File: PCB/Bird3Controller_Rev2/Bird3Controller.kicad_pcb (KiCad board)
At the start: 2 copper layers, 43 x 108 mm, 50 parts, among them J1 Bird 3 24-pin Connector, J2 TXW154028S0 Connector, J3 87832-2220, Q1 2N7002A, SW1 SW_Boot, SW2 SW_Reset, U1 ESP32-S3-WROOM-1, U3 SN65HVD231, U4 LMR36520ADDAR, U5 LM3519MK-20_NOPB

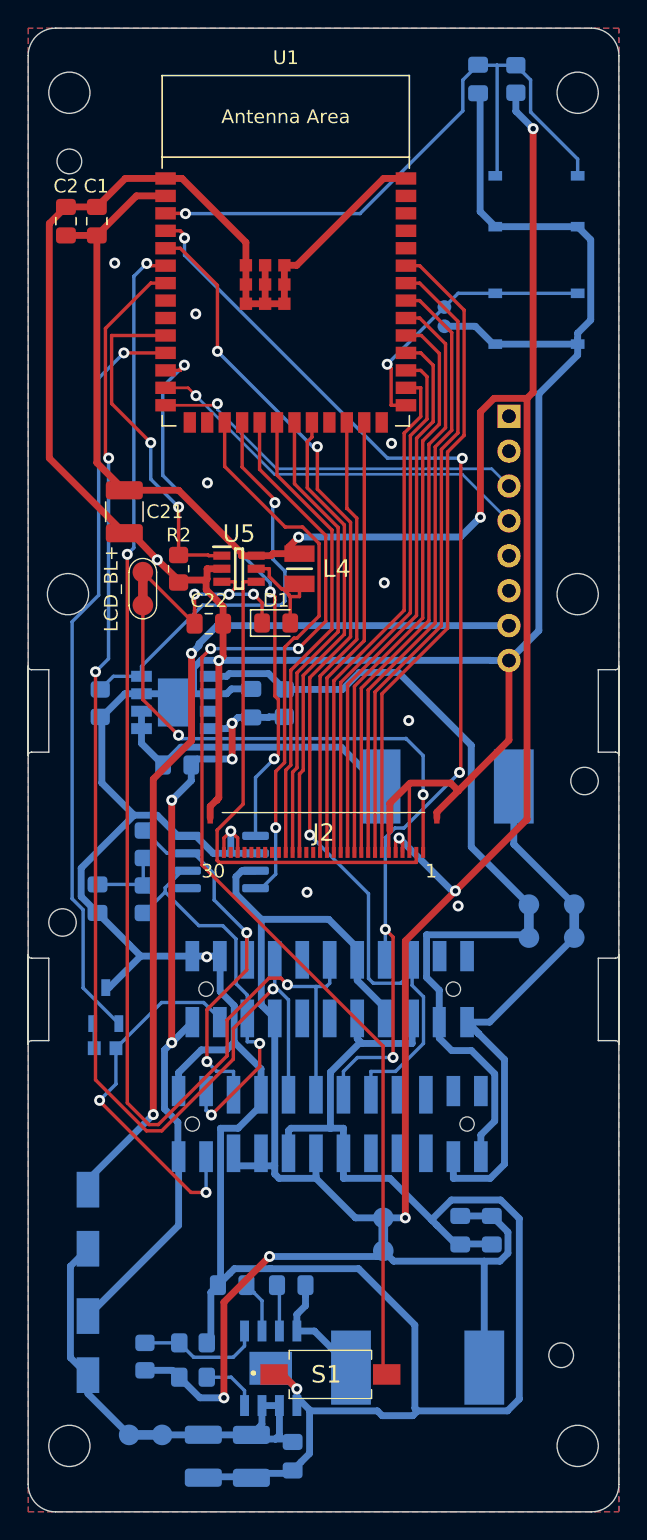
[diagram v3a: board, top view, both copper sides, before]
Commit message: Update PCB to use add PTC fuse on VIN
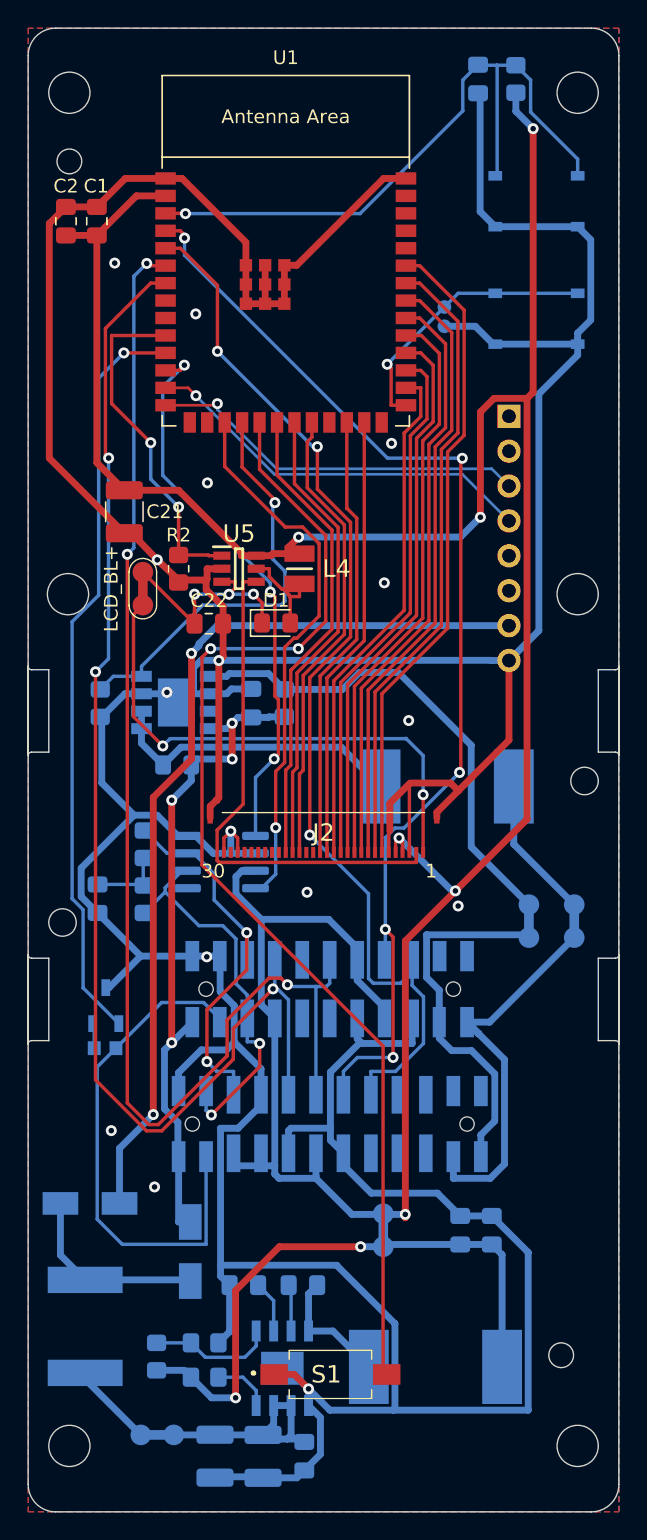
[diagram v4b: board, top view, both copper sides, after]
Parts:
- added F2: 0ZCF0100AF2A, Bird3Controller:FUSC7451X170N, B.Cu at (164.7, 136.5)
- moved D5 10.1 mm to (172.3, 131.1)
- moved L3 1.30 mm to (190.2, 139.4)
- moved D6 1.16 mm to (165.0, 127.5), turned to 0 degrees
- moved C14 0.85 mm to (177.6, 146.0)
- moved C15 0.85 mm to (180.6, 145.9)
- moved C16 0.85 mm to (174.1, 145.9)
- moved C17 0.85 mm to (176.2, 133.5)
- moved C19 0.85 mm to (180.5, 133.5)
- moved R11 0.85 mm to (173.3, 140.2)
- moved R12 0.85 mm to (169.8, 138.7)
- moved R13 0.85 mm to (173.3, 137.7)
- moved TP3 0.85 mm to (169.9, 144.4)
- moved U4 0.85 mm to (179.0, 139.6)
- moved TP2 0.30 mm to (186.3, 129.5)
- turned C18 to 90 degrees
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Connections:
- TP3 pad 2: Net-(D5-K) -> Net-(F2-Pad2)
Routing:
- net /PWR_ENA: track 27.2 -> 37.8 mm, vias 2 -> 0
- net GND: track 421.8 -> 412.2 mm, vias 13 -> 16
- net +36V: track 59.7 -> 50.1 mm
- net Net-(F2-Pad2): track 0.00 -> 6.19 mm
- net Net-(C18-Pad1): track 49.6 -> 43.7 mm
- net /LCD_BL+: track 36.0 -> 38.2 mm
- net Net-(D5-K): track 15.8 -> 14.0 mm

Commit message: Label USB connector pins
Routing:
- net +3V3: track 220.1 -> 220.9 mm
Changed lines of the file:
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@@
         (effects (font (size 1 1) (thickness 0.15)) (justify mirror))
+    )
+    (fp_text user "SBU1" (at 1.15 -2.55 unlocked) (layer "B.SilkS")
+        (effects (font (size 1 1) (thickness 0.25) bold) (justify left mirror))
+    )
+    (fp_text user "D-" (at 1.15 -7.65 unlocked) (layer "B.SilkS")
+        (effects (font (size 1 1) (thickness 0.25) bold) (justify left mirror))
+    )
+    (fp_text user "D+" (at 1.15 -5.1 unlocked) (layer "B.SilkS")
+        (effects (font (size 1 1) (thickness 0.25) bold) (justify left mirror))
+    )
+    (fp_text user "GND" (at 1.15 -17.85 unlocked) (layer "B.SilkS")
+        (effects (font (size 1 1) (thickness 0.25) bold) (justify left mirror))
+    )
+    (fp_text user "CC2" (at 1.15 0 unlocked) (layer "B.SilkS")
+        (effects (font (size 1 1) (thickness 0.25) bold) (justify left mirror))
+    )
+    (fp_text user "CC1" (at 1.15 -10.15 unlocked) (layer "B.SilkS")
+        (effects (font (size 1 1) (thickness 0.25) bold) (justify left mirror))
+    )
+    (fp_text user "+5V" (at 1.15 -15.25 unlocked) (layer "B.SilkS")
+        (effects (font (size 1 1) (thickness 0.25) bold) (justify left mirror))
+    )
+    (fp_text user "SBU2" (at 1.15 -12.7 unlocked) (layer "B.SilkS")
+        (effects (font (size 1 1) (thickness 0.25) bold) (justify left mirror))
+    )
+    (fp_text user "SBU1" (at 1.15 -2.55 unlocked) (layer "F.SilkS")
+        (effects (font (size 1 1) (thickness 0.25) bold) (justify right))
+    )
+    (fp_text user "+5V" (at 1.15 -15.25 unlocked) (layer "F.SilkS")
+        (effects (font (size 1 1) (thickness 0.25) bold) (justify right))
+    )
+    (fp_text user "D+" (at 1.15 -5.1 unlocked) (layer "F.SilkS")
+        (effects (font (size 1 1) (thickness 0.25) bold) (justify right))
+    )
+    (fp_text user "SBU2" (at 1.15 -12.7 unlocked) (layer "F.SilkS")
+        (effects (font (size 1 1) (thickness 0.25) bold) (justify right))
+    )
+    (fp_text user "D-" (at 1.15 -7.65 unlocked) (layer "F.SilkS")
+        (effects (font (size 1 1) (thickness 0.25) bold) (justify right))
+    )
+    (fp_text user "CC1" (at 1.15 -10.15 unlocked) (layer "F.SilkS")
+        (effects (font (size 1 1) (thickness 0.25) bold) (justify right))
+    )
+    (fp_text user "CC2" (at 1.15 0 unlocked) (layer "F.SilkS")
+        (effects (font (size 1 1) (thickness 0.25) bold) (justify right))
+    )
+    (fp_text user "GND" (at 1.15 -17.85 unlocked) (layer "F.SilkS")
+        (effects (font (size 1 1) (thickness 0.25) bold) (justify right))
     )
     (fp_text user "${REFERENCE}" (at 0 -8.89 90) (layer "B.Fab")
         (effects (font (size 1 1) (thickness 0.15)) (justify mirror))
     )
-    (fp_line (start -1.33 -19.11) (end 1.33 -19.11)
-      (stroke (width 0.12) (type solid)) (layer "B.SilkS"))
-    (fp_line (start -1.33 -1.27) (end -1.33 -19.11)
-      (stroke (width 0.12) (type solid)) (layer "B.SilkS"))
-    (fp_line (start -1.33 -1.27) (end 1.33 -1.27)
-      (stroke (width 0.12) (type solid)) (layer "B.SilkS"))
-    (fp_line (start -1.33 0) (end -1.33 1.33)
-      (stroke (width 0.12) (type solid)) (layer "B.SilkS"))
-    (fp_line (start -1.33 1.33) (end 0 1.33)
-      (stroke (width 0.12) (type solid)) (layer "B.SilkS"))
-    (fp_line (start 1.33 -1.27) (end 1.33 -19.11)
-      (stroke (width 0.12) (type solid)) (layer "B.SilkS"))
+    (fp_line (start -1.3 -19.1) (end 6.35 -19.1)
+      (stroke (width 0.12) (type solid)) (layer "B.SilkS"))
+    (fp_line (start -1.3 -1.25) (end -1.3 -19.1)
+      (stroke (width 0.12) (type solid)) (layer "B.SilkS"))
+    (fp_line (start -1.3 -1.25) (end 6.35 -1.25)
+      (stroke (width 0.12) (type solid)) (layer "B.SilkS"))
+    (fp_line (start -1.3 0) (end -1.3 1.33)
+      (stroke (width 0.12) (type solid)) (layer "B.SilkS"))
+    (fp_line (start -1.3 1.33) (end 0.03 1.33)
+      (stroke (width 0.12) (type solid)) (layer "B.SilkS"))
+    (fp_line (start 6.35 -1.25) (end 6.35 -19.1)
+      (stroke (width 0.12) (type solid)) (layer "B.SilkS"))
+    (fp_line (start -1.3 -19.1) (end 6.35 -19.1)
+      (stroke (width 0.12) (type solid)) (layer "F.SilkS"))
+    (fp_line (start -1.3 -1.25) (end -1.3 -19.1)
+      (stroke (width 0.12) (type solid)) (layer "F.SilkS"))
+    (fp_line (start -1.3 -1.25) (end 6.35 -1.25)
+      (stroke (width 0.12) (type solid)) (layer "F.SilkS"))
+    (fp_line (start -1.3 0) (end -1.3 1.33)
+      (stroke (width 0.12) (type solid)) (layer "F.SilkS"))
+    (fp_line (start -1.3 1.33) (end 0.03 1.33)
+      (stroke (width 0.12) (type solid)) (layer "F.SilkS"))
+    (fp_line (start 6.35 -1.25) (end 6.35 -19.1)
+      (stroke (width 0.12) (type solid)) (layer "F.SilkS"))
     (fp_line (start -1.8 -19.55) (end 1.8 -19.55)
       (stroke (width 0.05) (type solid)) (layer "B.CrtYd"))
@@
     (fp_line (start 1.27 -19.05) (end -1.27 -19.05)
       (stroke (width 0.1) (type solid)) (layer "B.Fab"))
-    (fp_line (start 1.27 1.27) (end 1.27 -19.05)
+    (fp_line (start 6.35 1.27) (end 6.35 -19.05)
       (stroke (width 0.1) (type solid)) (layer "B.Fab"))
     (pad "1" thru_hole rect (at 0 0 180) (size 1.7 1.7) (drill 1) (layers "*.Cu" "*.Mask")
@@
   (segment (start 190.25 99.0739) (end 191.812 97.5119) (width 0.5) (layer "F.Cu") (net 5))
   (via (at 166.55 122.25) (size 0.8) (drill 0.4) (layers "F.Cu" "B.Cu") (free) (net 5))
-  (via (at 191.8 105.9) (size 0.8) (drill 0.4) (layers "F.Cu" "B.Cu") (free) (net 5))
+  (via (at 193.65 106.05) (size 0.8) (drill 0.4) (layers "F.Cu" "B.Cu") (free) (net 5))
   (via (at 170.6 90.35) (size 0.8) (drill 0.4) (layers "F.Cu" "B.Cu") (net 5))
   (via (at 169.9 80.7) (size 0.8) (drill 0.4) (layers "F.Cu" "B.Cu") (net 5))
@@
   (segment (start 180.25 80.25) (end 179.474 80.25) (width 0.5) (layer "F.Cu") (net 9))
   (segment (start 178.327 80.25) (end 178.177 80.4) (width 0.5) (layer "F.Cu") (net 9))
+  (segment (start 193.42 69.9422) (end 194.414 68.9481) (width 0.5) (layer "F.Cu") (net 9))
   (segment (start 187.75 102) (end 187.75 101.4) (width 0.25) (layer "F.Cu") (net 9))
+  (segment (start 187.5 101.2) (end 187.7 101.4) (width 0) (layer "F.Cu") (net 9))
+  (segment (start 193.42 79.03) (end 193.42 69.9422) (width 0.5) (layer "F.Cu") (net 9))
+  (segment (start 191.6 104.8) (end 187.956 108.444) (width 0.5) (layer "F.Cu") (net 9))
   (segment (start 194.414 68.9481) (end 196.814 68.9481) (width 0.5) (layer "F.Cu") (net 9))
-  (segment (start 187.5 101.2) (end 187.7 101.4) (width 0) (layer "F.Cu") (net 9))
-  (segment (start 193.42 77.6) (end 193.42 69.9422) (width 0.5) (layer "F.Cu") (net 9))
-  (segment (start 191.6 104.8) (end 187.956 108.444) (width 0.5) (layer "F.Cu") (net 9))
   (segment (start 179.474 80.25) (end 178.327 80.25) (width 0.5) (layer "F.Cu") (net 9))
   (segment (start 165.5 57.0875) (end 163.25 57.0875) (width 0.5) (layer "F.Cu") (net 9))
@@
   (segment (start 165.5 57.0875) (end 165.5 73.6375) (width 0.5) (layer "F.Cu") (net 9))
   (segment (start 178.177 80.4) (end 177.1 80.4) (width 0.5) (layer "F.Cu") (net 9))
-  (segment (start 193.42 69.9422) (end 194.414 68.9481) (width 0.5) (layer "F.Cu") (net 9))
   (segment (start 179.474 79.765904) (end 180.188337 79.051567) (width 0.5) (layer "F.Cu") (net 9))
   (segment (start 187.956 108.444) (end 187.956 128.594) (width 0.5) (layer "F.Cu") (net 9))
@@
   (segment (start 176.023 80.4) (end 176.023 80.212) (width 0.5) (layer "F.Cu") (net 9))
   (segment (start 165.5 73.6375) (end 167.5 75.6375) (width 0.5) (layer "F.Cu") (net 9))
+  (segment (start 193.4 79.05) (end 193.42 79.03) (width 0.5) (layer "F.Cu") (net 9))
   (segment (start 176.023 80.212) (end 171.449 75.6375) (width 0.5) (layer "F.Cu") (net 9))
   (segment (start 197.258 68.5036) (end 197.258 49.3183) (width 0.5) (layer "F.Cu") (net 9))
@@
   (via (at 187.95 128.35) (size 0.8) (drill 0.4) (layers "F.Cu" "B.Cu") (net 9))
   (via (at 191.6 104.8) (size 0.8) (drill 0.4) (layers "F.Cu" "B.Cu") (net 9))
-  (via (at 193.42 77.6) (size 0.8) (drill 0.4) (layers "F.Cu" "B.Cu") (net 9))
+  (via (at 193.4 79.05) (size 0.8) (drill 0.4) (layers "F.Cu" "B.Cu") (net 9))
   (via (at 180.188337 79.051567) (size 0.8) (drill 0.4) (layers "F.Cu" "B.Cu") (net 9))
   (via (at 197.258 49.3183) (size 0.8) (drill 0.4) (layers "F.Cu" "B.Cu") (net 9))
   (via (at 187.5 100.95) (size 0.8) (drill 0.4) (layers "F.Cu" "B.Cu") (net 9))
+  (segment (start 193.4 79.05) (end 180.189904 79.05) (width 0.5) (layer "B.Cu") (net 9))
   (segment (start 177.471 106.871) (end 175.625 105.025) (width 0.5) (layer "B.Cu") (net 9))
+  (segment (start 180.189904 79.05) (end 180.188337 79.051567) (width 0.5) (layer "B.Cu") (net 9))
   (segment (start 181.45 125.548) (end 181.45 125.724) (width 0.5) (layer "B.Cu") (net 9))
   (segment (start 177.45 123.9) (end 177.45 124.812) (width 0.5) (layer "B.Cu") (net 9))
   (segment (start 197.258 49.308) (end 196 48.05) (width 0.5) (layer "B.Cu") (net 9))
-  (segment (start 191.9601 79.0399) (end 180.200004 79.0399) (width 0.5) (layer "B.Cu") (net 9))
-  (segment (start 193.42 77.6) (end 193.4 77.6) (width 0.5) (layer "B.Cu") (net 9))
   (segment (start 176.065 103.335) (end 177.05 103.335) (width 0.5) (layer "B.Cu") (net 9))
   (segment (start 197.258 49.3183) (end 197.258 49.308) (width 0.5) (layer "B.Cu") (net 9))
@@
   (segment (start 181.45 125.724) (end 178.763 125.724) (width 0.5) (layer "B.Cu") (net 9))
   (segment (start 196 48.05) (end 196 46.7) (width 0.5) (layer "B.Cu") (net 9))
-  (segment (start 193.4 77.6) (end 191.9601 79.0399) (width 0.5) (layer "B.Cu") (net 9))
   (segment (start 175.45 124.812) (end 177.45 124.812) (width 0.5) (layer "B.Cu") (net 9))
   (segment (start 186.35 128.6) (end 186.1 128.35) (width 0.5) (layer "B.Cu") (net 9))

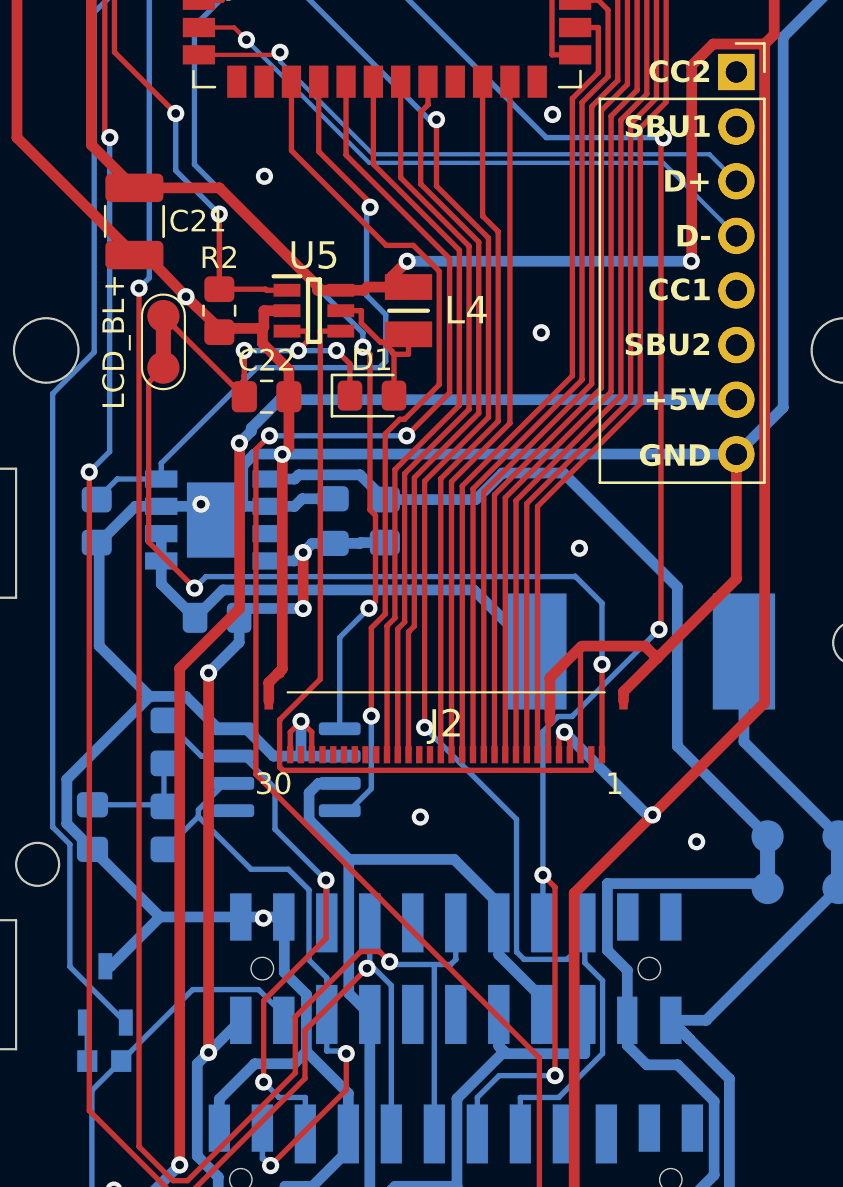
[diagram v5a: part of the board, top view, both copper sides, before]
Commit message: Rearrange some things to remove some vias
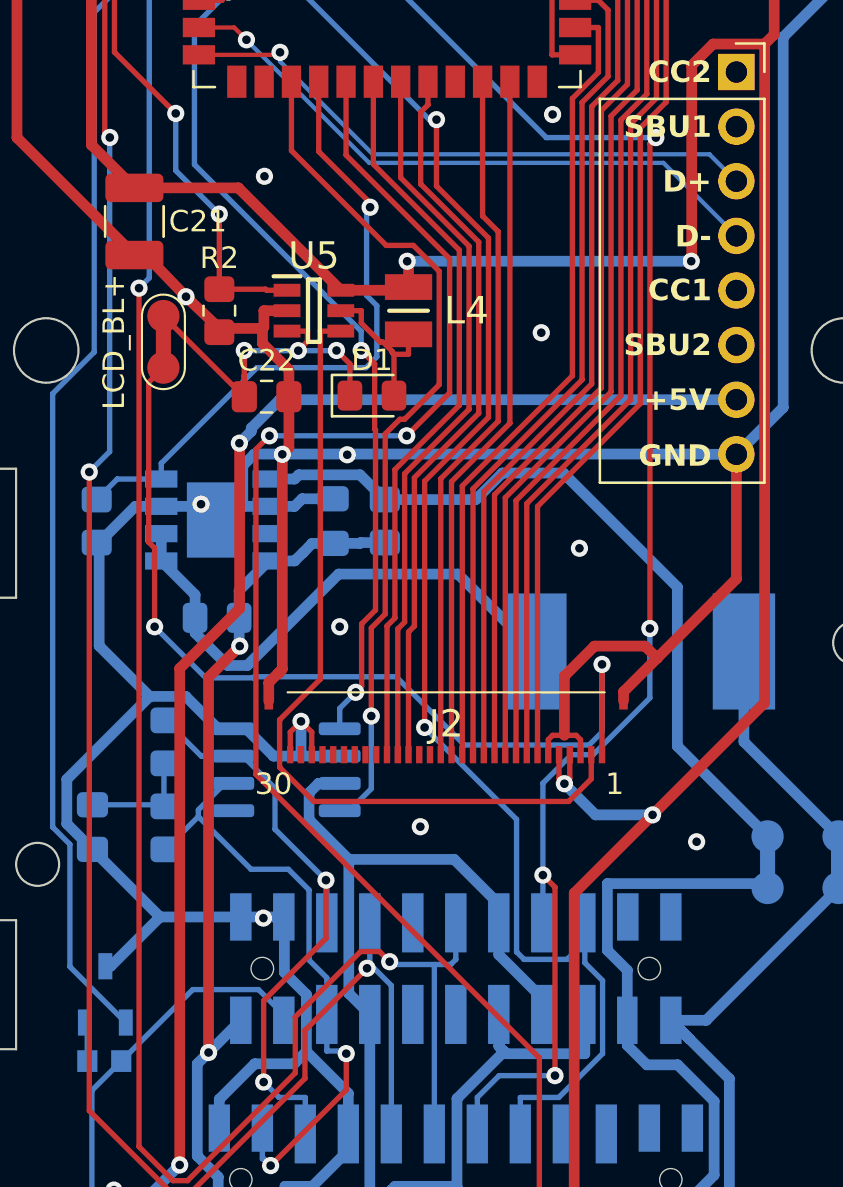
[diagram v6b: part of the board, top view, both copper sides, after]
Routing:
- net /LCD_BL+: track 38.2 -> 43.2 mm
- net GND: track 412.2 -> 408.8 mm, vias 16 -> 18
- net Net-(D3-A): track 22.1 -> 25.0 mm
- net +36V: track 50.1 -> 47.6 mm, vias 4 -> 2
- net /LCD_BL-: track 37.3 -> 38.7 mm
- net /LED_SIG: track 31.0 -> 30.3 mm
- net +3V3: track 220.9 -> 220.3 mm
